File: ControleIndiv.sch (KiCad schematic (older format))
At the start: 2 parts, among them Q4 IRLB3813PBF

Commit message: Placement canal passif intial
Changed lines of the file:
@@
 AR Path="/5EE1C393/5ED19A55" Ref="Q10"  Part="1"
 AR Path="/5EE3AA3B/5ED19A55" Ref="Q11"  Part="1"
-F 0 "Q11" H 7304 3696 50  0000 L CNN
+F 0 "Q4" H 7304 3696 50  0000 L CNN
 F 1 "IRLB3813PBF" H 7304 3605 50  0000 L CNN
 F 2 "PCB:TO-220-3_Horizontal_TabDown_AccessHole" H 7300 3750 50  0001 C CNN
@@
 AR Path="/5EE1C393/5EEECB97" Ref="R92"  Part="1"
 AR Path="/5EE3AA3B/5EEECB97" Ref="R93"  Part="1"
-F 0 "R93" H 6680 3854 50  0000 R CNN
+F 0 "R82" H 6680 3854 50  0000 R CNN
 F 1 "10k" H 6680 3945 50  0000 R CNN
 F 2 "Resistor_SMD:R_0603_1608Metric" V 6680 3900 50  0001 C CNN
@@
 AR Path="/5EE1C393/5EEECD87" Ref="#PWR0162"  Part="1"
 AR Path="/5EE3AA3B/5EEECD87" Ref="#PWR0164"  Part="1"
-F 0 "#PWR0164" H 7200 3850 50  0001 C CNN
+F 0 "#PWR0141" H 7200 3850 50  0001 C CNN
 F 1 "GNDA" H 7205 3927 50  0000 C CNN
 F 2 "" H 7200 4100 50  0001 C CNN
@@
 AR Path="/5EE1C393/5EEED08F" Ref="#PWR0161"  Part="1"
 AR Path="/5EE3AA3B/5EEED08F" Ref="#PWR0163"  Part="1"
-F 0 "#PWR0163" H 6750 3850 50  0001 C CNN
+F 0 "#PWR0140" H 6750 3850 50  0001 C CNN
 F 1 "GNDA" H 6755 3927 50  0000 C CNN
 F 2 "" H 6750 4100 50  0001 C CNN

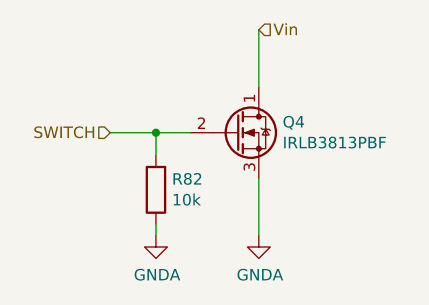
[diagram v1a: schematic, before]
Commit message: routing input canaux voltages
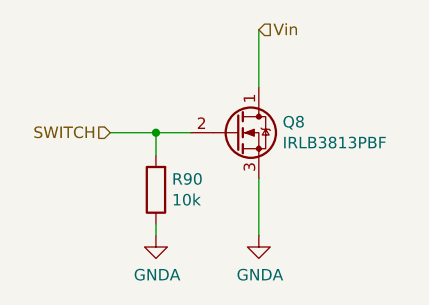
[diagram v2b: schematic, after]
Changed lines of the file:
@@
 $Descr A4 11693 8268
 encoding utf-8
-Sheet 43 80
+Sheet 51 80
 Title ""
 Date ""
@@
 AR Path="/5EE1C393/5ED19A55" Ref="Q10"  Part="1"
 AR Path="/5EE3AA3B/5ED19A55" Ref="Q11"  Part="1"
-F 0 "Q4" H 7304 3696 50  0000 L CNN
+F 0 "Q8" H 7304 3696 50  0000 L CNN
 F 1 "IRLB3813PBF" H 7304 3605 50  0000 L CNN
 F 2 "PCB:TO-220-3_Horizontal_TabDown_AccessHole" H 7300 3750 50  0001 C CNN
@@
 AR Path="/5EE1C393/5EEECB97" Ref="R92"  Part="1"
 AR Path="/5EE3AA3B/5EEECB97" Ref="R93"  Part="1"
-F 0 "R82" H 6680 3854 50  0000 R CNN
+F 0 "R90" H 6680 3854 50  0000 R CNN
 F 1 "10k" H 6680 3945 50  0000 R CNN
 F 2 "Resistor_SMD:R_0603_1608Metric" V 6680 3900 50  0001 C CNN
@@
 AR Path="/5EE1C393/5EEECD87" Ref="#PWR0162"  Part="1"
 AR Path="/5EE3AA3B/5EEECD87" Ref="#PWR0164"  Part="1"
-F 0 "#PWR0141" H 7200 3850 50  0001 C CNN
+F 0 "#PWR0164" H 7200 3850 50  0001 C CNN
 F 1 "GNDA" H 7205 3927 50  0000 C CNN
 F 2 "" H 7200 4100 50  0001 C CNN
@@
 AR Path="/5EE1C393/5EEED08F" Ref="#PWR0161"  Part="1"
 AR Path="/5EE3AA3B/5EEED08F" Ref="#PWR0163"  Part="1"
-F 0 "#PWR0140" H 6750 3850 50  0001 C CNN
+F 0 "#PWR0163" H 6750 3850 50  0001 C CNN
 F 1 "GNDA" H 6755 3927 50  0000 C CNN
 F 2 "" H 6750 4100 50  0001 C CNN
